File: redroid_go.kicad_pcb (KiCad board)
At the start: 2 copper layers, 70 x 95 mm, 100 parts, among them J1 USB4105-GF-A, J2 5051101892, J3 Conn_01x02_Pin, J4 Conn_01x10_Pin, Q1 UMH3N, Q2 PMOS, Q3 UMH3N, SW1 UP, SW10 A, SW11 SW_SPDT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

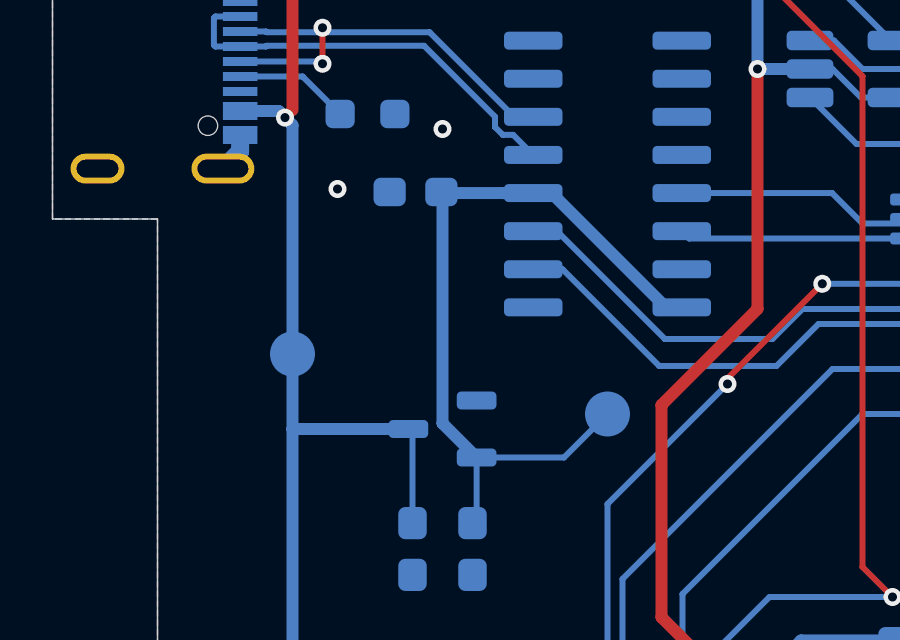
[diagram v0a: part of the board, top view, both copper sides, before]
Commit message: Move test pads
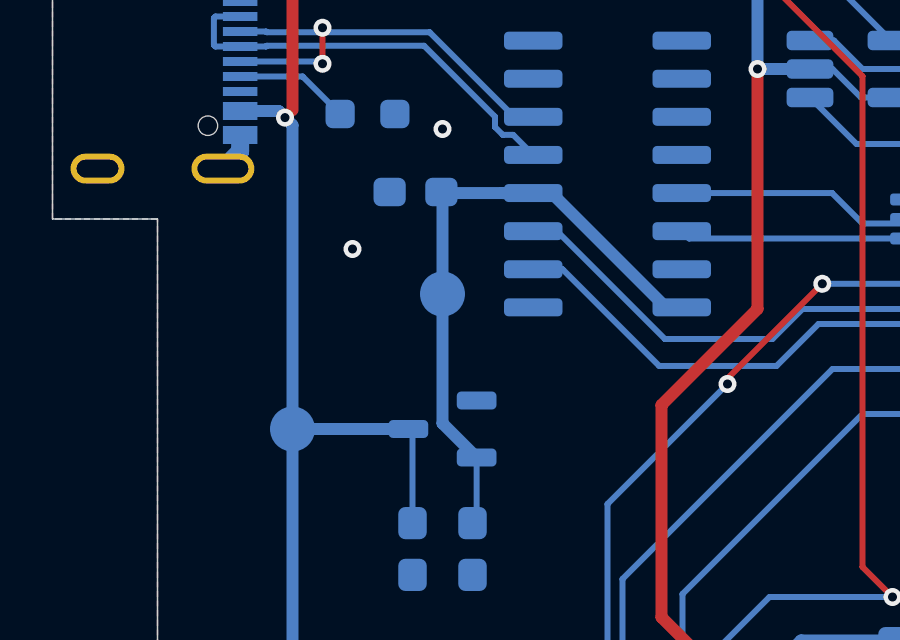
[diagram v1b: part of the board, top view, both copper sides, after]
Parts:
- moved TP15 6.80 mm to (141.5, 63.5)
- moved TP14 2.50 mm to (136.5, 68.0)
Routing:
- net P3V3_SERIAL: track 28.4 -> 23.5 mm
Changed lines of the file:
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@@
 	(footprint "TestPoint:TestPoint_Pad_D1.5mm"
 		(layer "B.Cu")
-		(at 136.5 65.5 180)
+		(at 136.5 68 180)
 		(descr "SMD pad as test Point, diameter 1.5mm")
 		(tags "test point SMD pad")
@@
 	(footprint "TestPoint:TestPoint_Pad_D1.5mm"
 		(layer "B.Cu")
-		(at 147 67.5 180)
+		(at 141.5 63.5 180)
 		(descr "SMD pad as test Point, diameter 1.5mm")
 		(tags "test point SMD pad")
 		(property "Reference" "TP15"
-			(at 0 -2 0)
+			(at 3 0 0)
 			(layer "B.SilkS")
 			(effects
@@
 	)
 	(via
-		(at 138 60)
+		(at 138.5 62)
 		(size 0.6)
 		(drill 0.3)
@@
 	)
 	(segment
-		(start 147 67.5)
-		(end 145.55 68.95)
-		(width 0.2)
-		(layer "B.Cu")
-		(net 112)
-	)
-	(segment
 		(start 141.5 60.1375)
 		(end 141.5 67.8125)
@@
 		(layer "B.Cu")
 		(net 112)
-	)
-	(segment
-		(start 145.55 68.95)
-		(end 142.6375 68.95)
-		(width 0.2)
-		(layer "B.Cu")
-		(net 112)

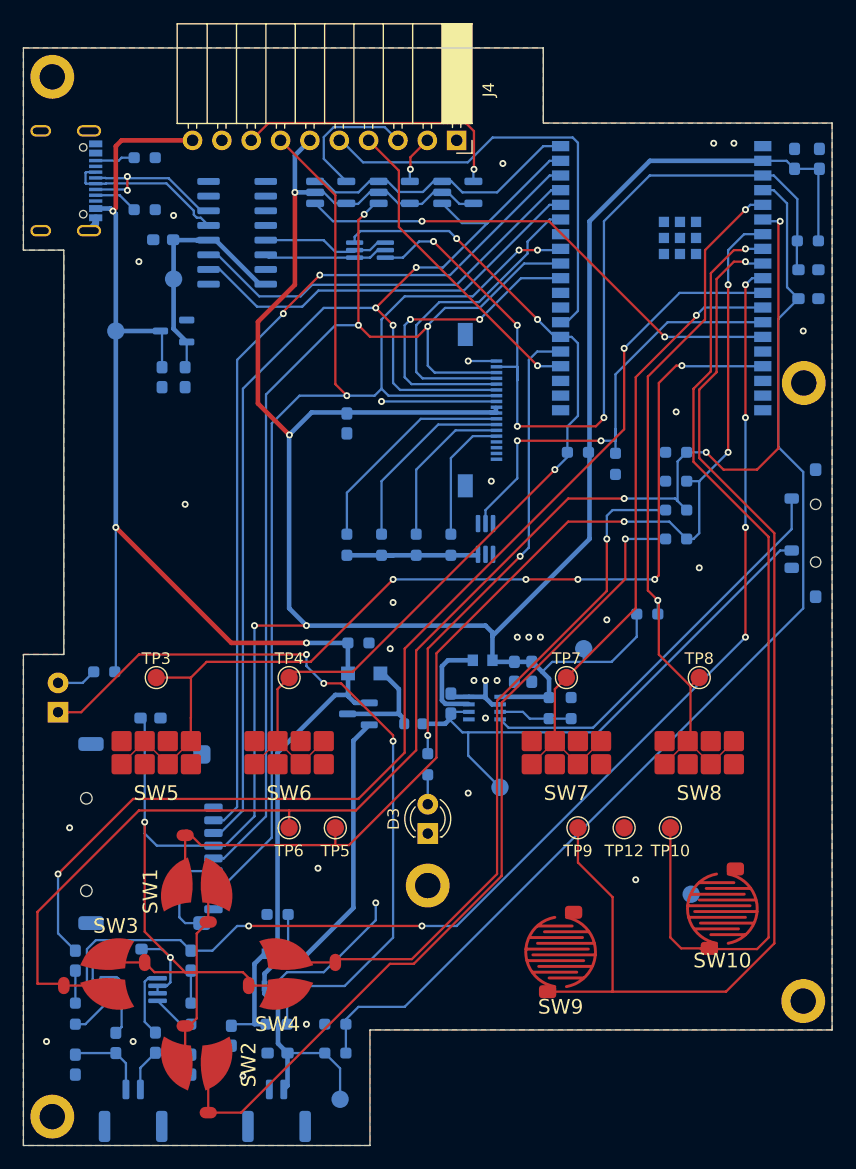
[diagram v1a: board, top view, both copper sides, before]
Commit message: Improve charge LED resistor
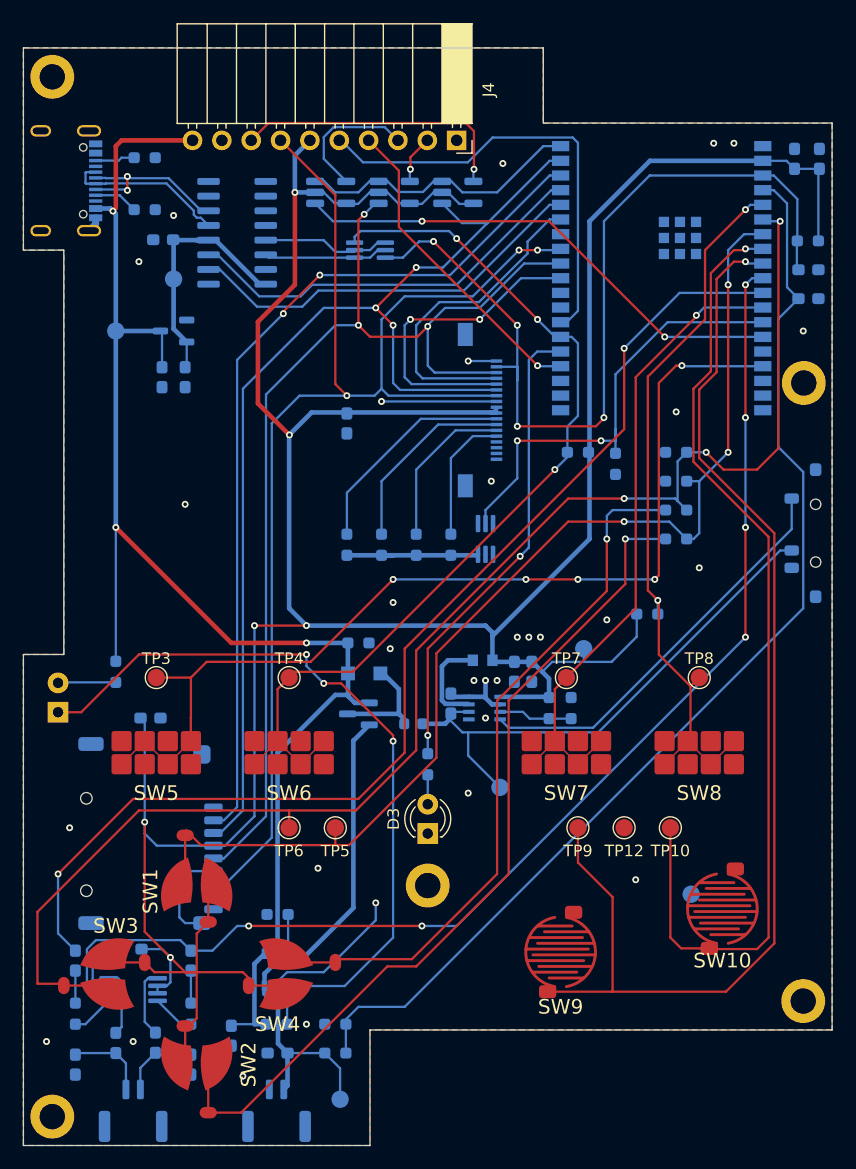
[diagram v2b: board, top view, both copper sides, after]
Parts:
- moved R8 1.00 mm to (136.5, 97.5), turned to -90 degrees
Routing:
- net Net-(D2-A): track 3.49 -> 5.02 mm
- net VBUS: track 128.0 -> 127.1 mm
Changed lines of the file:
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@@
 	(footprint "Resistor_SMD:R_0603_1608Metric_Pad0.98x0.95mm_HandSolder"
 		(layer "B.Cu")
-		(at 135.5 97.5 180)
+		(at 136.5 97.5 -90)
 		(descr "Resistor SMD 0603 (1608 Metric), square (rectangular) end terminal, IPC_7351 nominal with elongated pad for handsoldering. (Body size source: IPC-SM-782 page 72, https://www.pcb-3d.com/wordpress/wp-content/uploads/ipc-sm-782a_amendment_1_and_2.pdf), generated with kicad-footprint-generator")
 		(tags "resistor handsolder")
 		(property "Reference" "R8"
-			(at 0 1.5 0)
+			(at 0 1.5 90)
 			(layer "B.SilkS")
 			(effects
@@
 		)
 		(property "Value" "2k"
-			(at 0 -1.43 0)
+			(at 0 -1.43 90)
 			(layer "B.Fab")
 			(effects
@@
 		)
 		(property "Datasheet" ""
-			(at 0 0 0)
+			(at 0 0 90)
 			(unlocked yes)
 			(layer "B.Fab")
@@
 		)
 		(property "Description" "Resistor, US symbol"
-			(at 0 0 0)
+			(at 0 0 90)
 			(unlocked yes)
 			(layer "B.Fab")
@@
 		)
 		(fp_line
-			(start 1.65 0.73)
-			(end -1.65 0.73)
+			(start -1.65 0.73)
+			(end -1.65 -0.73)
 			(stroke
 				(width 0.05)
@@
 		)
 		(fp_line
-			(start 1.65 -0.73)
-			(end 1.65 0.73)
+			(start 1.65 0.73)
+			(end -1.65 0.73)
 			(stroke
 				(width 0.05)
@@
 		)
 		(fp_line
-			(start -1.65 0.73)
-			(end -1.65 -0.73)
+			(start -1.65 -0.73)
+			(end 1.65 -0.73)
 			(stroke
 				(width 0.05)
@@
 		)
 		(fp_line
-			(start -1.65 -0.73)
-			(end 1.65 -0.73)
+			(start 1.65 -0.73)
+			(end 1.65 0.73)
 			(stroke
 				(width 0.05)
@@
 		)
 		(fp_line
-			(start 0.8 0.4125)
-			(end -0.8 0.4125)
+			(start -0.8 0.4125)
+			(end -0.8 -0.4125)
 			(stroke
 				(width 0.1)
@@
 		)
 		(fp_line
-			(start 0.8 -0.4125)
-			(end 0.8 0.4125)
+			(start 0.8 0.4125)
+			(end -0.8 0.4125)
 			(stroke
 				(width 0.1)
@@
 		)
 		(fp_line
-			(start -0.8 0.4125)
-			(end -0.8 -0.4125)
+			(start -0.8 -0.4125)
+			(end 0.8 -0.4125)
 			(stroke
 				(width 0.1)
@@
 		)
 		(fp_line
-			(start -0.8 -0.4125)
-			(end 0.8 -0.4125)
+			(start 0.8 -0.4125)
+			(end 0.8 0.4125)
 			(stroke
 				(width 0.1)
@@
 		)
 		(fp_text user "${REFERENCE}"
-			(at 0 0 0)
+			(at 0 0 90)
 			(layer "B.Fab")
 			(effects
@@
 		)
 		(pad "1" smd roundrect
-			(at -0.9125 0 180)
+			(at -0.9125 0 270)
 			(size 0.975 0.95)
 			(layers "B.Cu" "B.Mask" "B.Paste")
@@
 		)
 		(pad "2" smd roundrect
-			(at 0.9125 0 180)
+			(at 0.9125 0 270)
 			(size 0.975 0.95)
 			(layers "B.Cu" "B.Mask" "B.Paste")
@@
 	)
 	(segment
+		(start 136.5 96.5875)
+		(end 136.5 85)
+		(width 0.2)
+		(layer "B.Cu")
+		(net 5)
+	)
+	(segment
 		(start 156.5875 95)
 		(end 156.5875 97.627949)
@@
 	)
 	(segment
-		(start 136.5 97.4125)
-		(end 136.5 85)
-		(width 0.2)
-		(layer "B.Cu")
-		(net 5)
-	)
-	(segment
 		(start 156.5875 95)
 		(end 153 95)
@@
 	)
 	(segment
-		(start 136.4125 97.5)
-		(end 136.5 97.4125)
-		(width 0.2)
-		(layer "B.Cu")
-		(net 5)
-	)
-	(segment
 		(start 156.6 99.5)
 		(end 156.6 99.6)
@@
 	)
 	(segment
-		(start 134.5875 97.5)
-		(end 133.6275 98.46)
+		(start 136.5 98.4125)
+		(end 131.5475 98.4125)
 		(width 0.2)
 		(layer "B.Cu")
@@
 	)
 	(segment
-		(start 133.6275 98.46)
+		(start 131.5475 98.4125)
 		(end 131.5 98.46)
 		(width 0.2)
@@
 	)
 	(segment
-		(start 180.6 89.4671)
-		(end 169.901 100.1661)
+		(start 162.5 123)
+		(end 159.999999 123)
 		(width 0.2)
 		(layer "F.Cu")
@@
 	)
 	(segment
-		(start 162.293942 122.773158)
-		(end 160.226841 122.773158)
+		(start 180.6 86)
+		(end 180.6 89.9)
 		(width 0.2)
 		(layer "F.Cu")
@@
 	)
 	(segment
-		(start 169.901 115.1661)
-		(end 162.293942 122.773158)
+		(start 170.5 115)
+		(end 162.5 123)
 		(width 0.2)
 		(layer "F.Cu")
@@
 	)
 	(segment
-		(start 169.901 100.1661)
-		(end 169.901 115.1661)
+		(start 144.901 135.655)
+		(end 147.344999 135.655)
 		(width 0.2)
 		(layer "F.Cu")
@@
 	)
 	(segment
-		(start 160.226841 122.773158)
-		(end 147.344999 135.655)
+		(start 180.6 89.9)
+		(end 170.5 100)
 		(width 0.2)
 		(layer "F.Cu")
@@
 	)
 	(segment
-		(start 144.901 135.655)
-		(end 147.344999 135.655)
+		(start 170.5 100)
+		(end 170.5 115)
 		(width 0.2)
 		(layer "F.Cu")
@@
 	)
 	(segment
-		(start 180.6 86)
-		(end 180.6 89.4671)
+		(start 147.344999 135.655)
+		(end 159.999999 123)
 		(width 0.2)
 		(layer "F.Cu")
@@
 	)
 	(segment
-		(start 179 86)
-		(end 179 90.5)
+		(start 169.5 115.000001)
+		(end 162.127843 122.372158)
 		(width 0.2)
 		(layer "F.Cu")
@@
 	)
 	(segment
-		(start 169.5 100)
-		(end 169.5 115)
+		(start 162.127843 122.372158)
+		(end 155.782843 122.372158)
 		(width 0.2)
 		(layer "F.Cu")
@@
 	)
 	(segment
-		(start 162.127842 122.372158)
-		(end 155.782843 122.372158)
+		(start 179 90.5)
+		(end 169.5 100)
 		(width 0.2)
 		(layer "F.Cu")
@@
 	)
 	(segment
-		(start 179 90.5)
-		(end 169.5 100)
+		(start 169.5 100)
+		(end 169.5 115.000001)
 		(width 0.2)
 		(layer "F.Cu")
@@
 	)
 	(segment
-		(start 169.5 115)
-		(end 162.127842 122.372158)
+		(start 179 86)
+		(end 179 90.5)
 		(width 0.2)
 		(layer "F.Cu")

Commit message: Various fixes
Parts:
- moved R19 1.50 mm to (161.0, 86.5)
- moved R24 1.50 mm to (155.0, 86.5)
- moved R25 1.50 mm to (158.0, 86.5)
- moved R26 1.50 mm to (164.0, 86.5)
- moved R15 1.00 mm to (181.5, 92.5), turned to -90 degrees
- moved R18 0.50 mm to (163.5, 106.0)
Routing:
- net Net-(D3-A): track 2.91 -> 2.05 mm
- net IO39: track 54.9 -> 55.7 mm
- net Net-(J2-LEDK2): track 16.6 -> 17.2 mm
- net Net-(J2-LEDK1): track 19.2 -> 19.8 mm
- net Net-(J2-LEDK3): track 13.9 -> 14.6 mm
- net Net-(J2-LEDK4): track 11.3 -> 11.9 mm
- net IO2: track 40.7 -> 41.3 mm
- net GND: vias 31 -> 37
